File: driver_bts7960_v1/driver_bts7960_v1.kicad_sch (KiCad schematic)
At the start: 25 parts, among them J1 Motor_1, J6 Motor_2, J7 Conn_02x04_Odd_Even, U1 BTS7960B, U2 BTS7960B, U3 BTS7960B, U4 BTS7960B

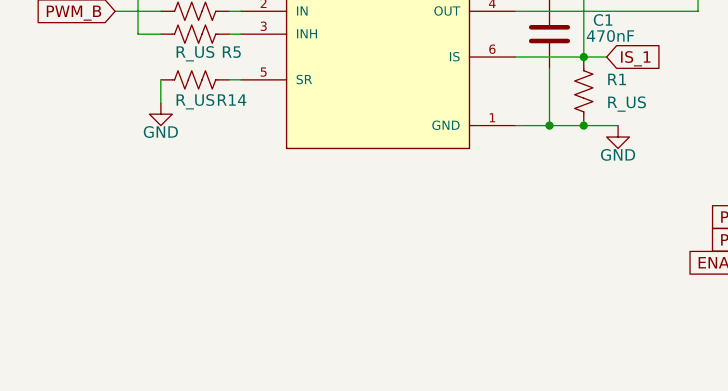
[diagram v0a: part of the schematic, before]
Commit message: driver bts7960 v1
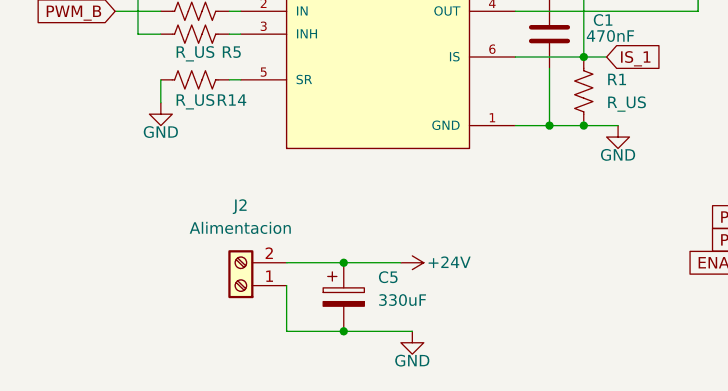
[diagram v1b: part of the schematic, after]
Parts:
- added C5: 330uF, Capacitor_THT:CP_Radial_D8.0mm_P3.80mm, symbol Device:C_Polarized
- added J2: Alimentacion, Connector_AMASS:AMASS_XT30UPB-F_1x02_P5.0mm_Vertical, symbol Connector:Screw_Terminal_01x02
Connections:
- net +24V: now also C5.1, J2.2 (Pin_2)
- net GND: now also C5.2, J2.1 (Pin_1)

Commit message: .
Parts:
- C5: footprint Capacitor_THT:CP_Radial_D8.0mm_P3.80mm -> Capacitor_THT:CP_Radial_D10.0mm_P5.00mm
- J1, J6: footprint Connector_AMASS:AMASS_XT30PW-M_1x02_P2.50mm_Horizontal -> Connector_AMASS:AMASS_XT30U-F_1x02_P5.0mm_Vertical
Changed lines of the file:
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@@
 			)
 		)
-		(property "Footprint" "Capacitor_THT:CP_Radial_D8.0mm_P3.80mm"
+		(property "Footprint" "Capacitor_THT:CP_Radial_D10.0mm_P5.00mm"
 			(at 67.0052 101.6 0)
 			(effects
@@
 			)
 		)
-		(property "Footprint" "Connector_AMASS:AMASS_XT30PW-M_1x02_P2.50mm_Horizontal"
+		(property "Footprint" "Connector_AMASS:AMASS_XT30U-F_1x02_P5.0mm_Vertical"
 			(at 215.9 49.53 0)
 			(effects
@@
 			)
 		)
-		(property "Footprint" "Connector_AMASS:AMASS_XT30PW-M_1x02_P2.50mm_Horizontal"
+		(property "Footprint" "Connector_AMASS:AMASS_XT30U-F_1x02_P5.0mm_Vertical"
 			(at 116.84 49.53 0)
 			(effects

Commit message: .
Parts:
- removed J7: Conn_02x04_Odd_Even, Connector_PinHeader_2.54mm:PinHeader_2x04_P2.54mm_Horizontal, symbol Connector_Generic:Conn_02x04_Odd_Even
- added J3: Conn_02x03_Odd_Even, Connector_PinHeader_2.54mm:PinHeader_2x03_P2.54mm_Horizontal, symbol Connector_Generic:Conn_02x03_Odd_Even
- added U5: 74HC244, Package_SO:SSOP-20_4.4x6.5mm_P0.65mm, symbol 74xx:74HC244
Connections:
- net ENABLE_1: now also J3.5 (Pin_5)
- net ENABLE_2: now also J3.6 (Pin_6)
- net GND: now also U5.10 (GND), U5.11 (2A3), U5.13 (2A2), U5.15 (2A1), U5.17 (2A0), U5.3 (2Y0), U5.5 (2Y1), U5.7 (2Y2), U5.9 (2Y3)
- net PWM_A: now also J3.1 (Pin_1), U5.2 (1A0); no longer R3.2
- net PWM_B: now also J3.3 (Pin_3), U5.4 (1A1); no longer R2.2
- net PWM_C: now also J3.2 (Pin_2), U5.6 (1A2); no longer R6.2
- net PWM_D: now also J3.4 (Pin_4), U5.8 (1A3); no longer R8.2
- net IS_1: no longer names the net of R1.1, U1.6 (IS), U2.6 (IS)
- net IS_2: no longer names the net of R10.1, U3.6 (IS), U4.6 (IS)
- new net +5V: U5.20 (VCC)
- new net OUT_A: R3.2, U5.18 (1Y0)
- new net OUT_B: R2.2, U5.16 (1Y1)
- new net OUT_C: R6.2, U5.14 (1Y2)
- new net OUT_D: R8.2, U5.12 (1Y3)

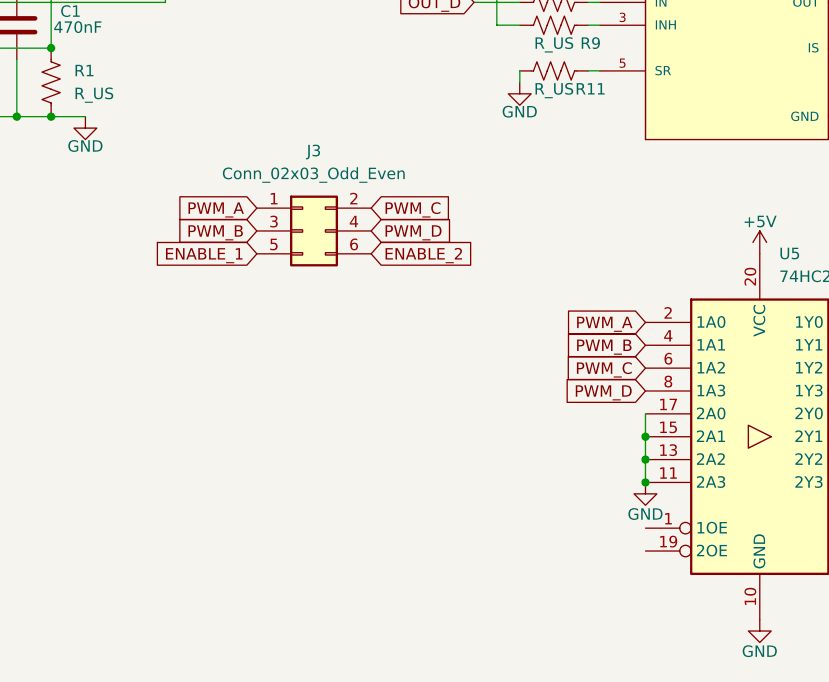
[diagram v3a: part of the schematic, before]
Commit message: v2 terminado con 74hc244
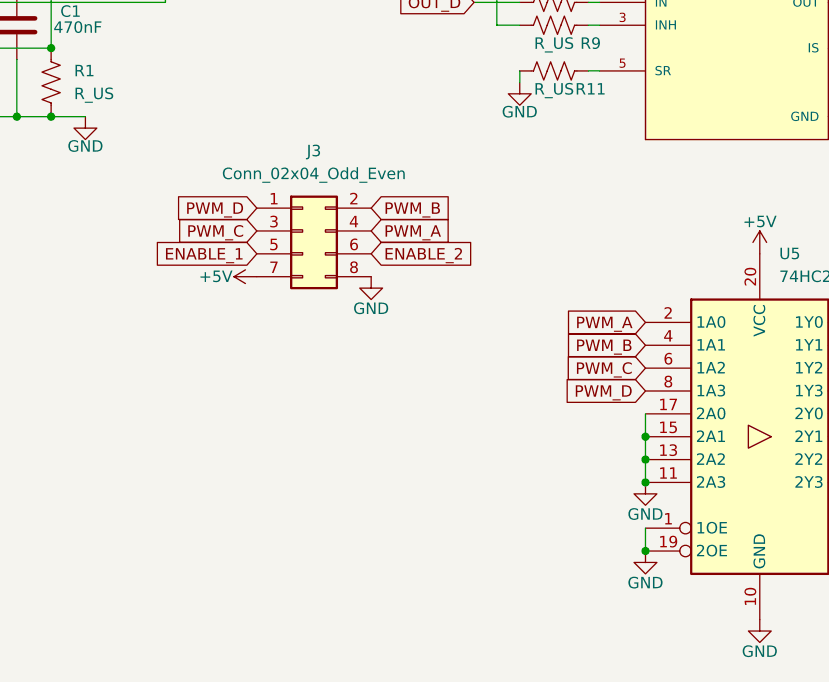
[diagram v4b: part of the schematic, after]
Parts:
- removed J3: Conn_02x03_Odd_Even, Connector_PinHeader_2.54mm:PinHeader_2x03_P2.54mm_Horizontal, symbol Connector_Generic:Conn_02x03_Odd_Even
- added J3: Conn_02x04_Odd_Even, Connector_PinHeader_2.54mm:PinHeader_2x04_P2.54mm_Vertical, symbol Connector_Generic:Conn_02x04_Odd_Even
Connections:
- net +5V: now also J3.7 (Pin_7)
- net ENABLE_1: now also J3.5 (Pin_5)
- net ENABLE_2: now also J3.6 (Pin_6)
- net GND: now also U5.1 (1OE), U5.19 (2OE), J3.8 (Pin_8)
- net PWM_A: now also J3.4 (Pin_4)
- net PWM_B: now also J3.2 (Pin_2)
- net PWM_C: now also J3.3 (Pin_3)
- net PWM_D: now also J3.1 (Pin_1)

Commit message: .
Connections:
- net ENABLE_1: now also U5.17 (2A0); no longer R4.2, R5.2
- net ENABLE_2: now also U5.15 (2A1); no longer R7.2, R9.2
- net GND: no longer U5.15 (2A1), U5.17 (2A0), U5.3 (2Y0), U5.5 (2Y1)
- new net OUT_EN_1: R4.2, R5.2, U5.3 (2Y0)
- new net OUT_EN_2: R7.2, R9.2, U5.5 (2Y1)
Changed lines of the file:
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@@
-	)
-	(junction
-		(at 184.15 114.3)
-		(diameter 0)
-		(color 0 0 0 0)
 	)
 	(junction
@@
 	)
 	(junction
-		(at 184.15 116.84)
-		(diameter 0)
-		(color 0 0 0 0)
-	)
-	(junction
 		(at 184.15 119.38)
 		(diameter 0)
@@
 	)
 	(junction
-		(at 158.75 116.84)
-		(diameter 0)
-		(color 0 0 0 0)
-	)
-	(junction
 		(at 92.71 71.12)
 		(diameter 0)
@@
 	)
 	(junction
-		(at 158.75 114.3)
-		(diameter 0)
-		(color 0 0 0 0)
-	)
-	(junction
 		(at 158.75 119.38)
 		(diameter 0)
@@
 	(wire
 		(pts
-			(xy 144.78 39.37) (xy 142.24 39.37)
-		)
-		(stroke
-			(width 0)
-			(type default)
-		)
-	)
-	(wire
-		(pts
 			(xy 53.34 68.58) (xy 54.61 68.58)
 		)
@@
 	(wire
 		(pts
-			(xy 158.75 111.76) (xy 158.75 114.3)
-		)
-		(stroke
-			(width 0)
-			(type default)
-		)
-	)
-	(wire
-		(pts
 			(xy 204.47 66.04) (xy 204.47 52.07)
 		)
@@
 	(wire
 		(pts
-			(xy 142.24 68.58) (xy 144.78 68.58)
-		)
-		(stroke
-			(width 0)
-			(type default)
-		)
-	)
-	(wire
-		(pts
 			(xy 153.67 39.37) (xy 152.4 39.37)
 		)
@@
 	(wire
 		(pts
-			(xy 43.18 39.37) (xy 43.18 68.58)
-		)
-		(stroke
-			(width 0)
-			(type default)
-		)
-	)
-	(wire
-		(pts
 			(xy 204.47 49.53) (xy 210.82 49.53)
 		)
@@
 	(wire
 		(pts
-			(xy 43.18 68.58) (xy 45.72 68.58)
-		)
-		(stroke
-			(width 0)
-			(type default)
-		)
-	)
-	(wire
-		(pts
 			(xy 187.96 60.96) (xy 187.96 64.77)
 		)
@@
 	(wire
 		(pts
-			(xy 45.72 39.37) (xy 43.18 39.37)
-		)
-		(stroke
-			(width 0)
-			(type default)
-		)
-	)
-	(wire
-		(pts
-			(xy 142.24 39.37) (xy 142.24 68.58)
-		)
-		(stroke
-			(width 0)
-			(type default)
-		)
-	)
-	(wire
-		(pts
 			(xy 152.4 68.58) (xy 153.67 68.58)
 		)
@@
 	(wire
 		(pts
-			(xy 184.15 114.3) (xy 184.15 116.84)
-		)
-		(stroke
-			(width 0)
-			(type default)
-		)
-	)
-	(wire
-		(pts
-			(xy 158.75 114.3) (xy 158.75 116.84)
-		)
-		(stroke
-			(width 0)
-			(type default)
-		)
-	)
-	(wire
-		(pts
 			(xy 184.15 41.91) (xy 191.77 41.91)
 		)
@@
 	(wire
 		(pts
-			(xy 184.15 111.76) (xy 184.15 114.3)
-		)
-		(stroke
-			(width 0)
-			(type default)
-		)
-	)
-	(wire
-		(pts
 			(xy 88.9 31.75) (xy 85.09 31.75)
 		)
@@
 		)
 	)
+	(global_label "OUT_EN_2"
+		(shape input)
+		(at 184.15 114.3 0)
+		(fields_autoplaced yes)
+		(effects
+			(font
+				(size 1.27 1.27)
+			)
+			(justify left)
+		)
+		(property "Intersheetrefs" "${INTERSHEET_REFS}"
+			(at 196.388 114.3 0)
+			(hide yes)
+			(show_name no)
+			(do_not_autoplace no)
+			(effects
+				(font
+					(size 1.27 1.27)
+				)
+				(justify left)
+			)
+		)
+	)
 	(global_label "OUT_D"
 		(shape input)
@@
 		)
 	)
+	(global_label "OUT_EN_1"
+		(shape input)
+		(at 45.72 68.58 180)
+		(fields_autoplaced yes)
+		(effects
+			(font
+				(size 1.27 1.27)
+			)
+			(justify right)
+		)
+		(property "Intersheetrefs" "${INTERSHEET_REFS}"
+			(at 33.482 68.58 0)
+			(hide yes)
+			(show_name no)
+			(do_not_autoplace no)
+			(effects
+				(font
+					(size 1.27 1.27)
+				)
+				(justify right)
+			)
+		)
+	)
 	(global_label "PWM_B"
 		(shape input)
@@
 		)
 	)
+	(global_label "ENABLE_1"
+		(shape input)
+		(at 158.75 111.76 180)
+		(fields_autoplaced yes)
+		(effects
+			(font
+				(size 1.27 1.27)
+			)
+			(justify right)
+		)
+		(property "Intersheetrefs" "${INTERSHEET_REFS}"
+			(at 146.5725 111.76 0)
+			(hide yes)
+			(show_name no)
+			(do_not_autoplace no)
+			(effects
+				(font
+					(size 1.27 1.27)
+				)
+				(justify right)
+			)
+		)
+	)
 	(global_label "OUT_B"
 		(shape input)
@@
 		)
 	)
-	(global_label "ENABLE_1"
-		(shape input)
-		(at 43.18 53.34 180)
-		(fields_autoplaced yes)
-		(effects
-			(font
-				(size 1.27 1.27)
-			)
-			(justify right)
-		)
-		(property "Intersheetrefs" "${INTERSHEET_REFS}"
-			(at 31.0025 53.34 0)
+	(global_label "OUT_EN_2"
+		(shape input)
+		(at 144.78 68.58 180)
+		(fields_autoplaced yes)
+		(effects
+			(font
+				(size 1.27 1.27)
+			)
+			(justify right)
+		)
+		(property "Intersheetrefs" "${INTERSHEET_REFS}"
+			(at 132.542 68.58 0)
+			(hide yes)
+			(show_name no)
+			(do_not_autoplace no)
+			(effects
+				(font
+					(size 1.27 1.27)
+				)
+				(justify right)
+			)
+		)
+	)
+	(global_label "OUT_EN_1"
+		(shape input)
+		(at 45.72 39.37 180)
+		(fields_autoplaced yes)
+		(effects
+			(font
+				(size 1.27 1.27)
+			)
+			(justify right)
+		)
+		(property "Intersheetrefs" "${INTERSHEET_REFS}"
+			(at 33.482 39.37 0)
 			(hide yes)
 			(show_name no)
@@
 		)
 	)
+	(global_label "ENABLE_2"
+		(shape input)
+		(at 158.75 114.3 180)
+		(fields_autoplaced yes)
+		(effects
+			(font
+				(size 1.27 1.27)
+			)
+			(justify right)
+		)
+		(property "Intersheetrefs" "${INTERSHEET_REFS}"
+			(at 146.5725 114.3 0)
+			(hide yes)
+			(show_name no)
+			(do_not_autoplace no)
+			(effects
+				(font
+					(size 1.27 1.27)
+				)
+				(justify right)
+			)
+		)
+	)
 	(global_label "PWM_C"
 		(shape input)
@@
 		)
 	)
-	(global_label "ENABLE_2"
-		(shape input)
-		(at 142.24 53.34 180)
-		(fields_autoplaced yes)
-		(effects
-			(font
-				(size 1.27 1.27)
-			)
-			(justify right)
-		)
-		(property "Intersheetrefs" "${INTERSHEET_REFS}"
-			(at 130.0625 53.34 0)
-			(hide yes)
-			(show_name no)
+	(global_label "OUT_EN_1"
+		(shape input)
+		(at 184.15 111.76 0)
+		(fields_autoplaced yes)
+		(effects
+			(font
+				(size 1.27 1.27)
+			)
+			(justify left)
+		)
+		(property "Intersheetrefs" "${INTERSHEET_REFS}"
+			(at 196.388 111.76 0)
+			(hide yes)
+			(show_name no)
+			(do_not_autoplace no)
+			(effects
+				(font
+					(size 1.27 1.27)
+				)
+				(justify left)
+			)
+		)
+	)
+	(global_label "OUT_EN_2"
+		(shape input)
+		(at 144.78 39.37 180)
+		(fields_autoplaced yes)
+		(effects
+			(font
+				(size 1.27 1.27)
+			)
+			(justify right)
+		)
+		(property "Intersheetrefs" "${INTERSHEET_REFS}"
+			(at 132.542 39.37 0)
+			(hide yes)
+			(show_name no)

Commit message: .
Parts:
- removed J3: Conn_02x04_Odd_Even, Connector_PinHeader_2.54mm:PinHeader_2x04_P2.54mm_Vertical, symbol Connector_Generic:Conn_02x04_Odd_Even
- added J7: Conn_02x04_Odd_Even, Connector_PinHeader_2.54mm:PinHeader_2x04_P2.54mm_Vertical, symbol Connector_Generic:Conn_02x04_Odd_Even
- C5: footprint Capacitor_THT:CP_Radial_D10.0mm_P5.00mm -> Capacitor_THT:CP_Radial_D8.0mm_P3.80mm
- J2: value Alimentacion -> XT30; footprint Connector_AMASS:AMASS_XT30UPB-F_1x02_P5.0mm_Vertical -> Connector_AMASS:AMASS_XT30U-F_1x02_P5.0mm_Vertical
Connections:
- net +5V: now also J7.7 (Pin_7)
- net ENABLE_1: now also J7.5 (Pin_5)
- net ENABLE_2: now also J7.6 (Pin_6)
- net GND: now also J7.8 (Pin_8)
- net PWM_A: now also J7.4 (Pin_4)
- net PWM_B: now also J7.2 (Pin_2)
- net PWM_C: now also J7.1 (Pin_1)
- net PWM_D: now also J7.3 (Pin_3)
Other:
- note added: "Control de motores"
- note added: "Entrada VCC"
- note added: "Integrado 74hc244"
- note added: "Pines de entrada"
- moved on the sheet: C1, C2, C3, C4, C5, J1, J2, J6, R1, R10, R11, R12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

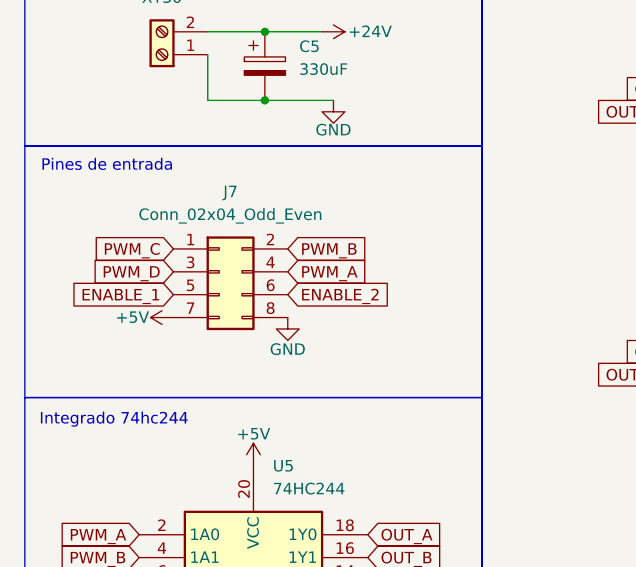
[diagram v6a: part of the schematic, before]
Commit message: footprint 74hc244 corregido
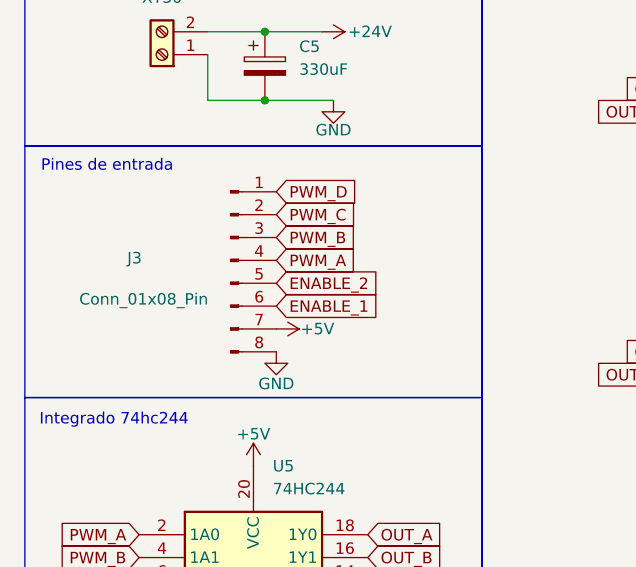
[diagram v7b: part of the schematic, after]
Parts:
- removed J7: Conn_02x04_Odd_Even, Connector_PinHeader_2.54mm:PinHeader_2x04_P2.54mm_Vertical, symbol Connector_Generic:Conn_02x04_Odd_Even
- added J3: Conn_01x08_Pin, Connector_PinHeader_2.54mm:PinHeader_1x08_P2.54mm_Vertical, symbol Connector:Conn_01x08_Pin
- U5: footprint Package_SO:SSOP-20_4.4x6.5mm_P0.65mm -> 74HC244D_653:SOIC127P1032X265-20N
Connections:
- net +5V: now also J3.7 (Pin_7)
- net ENABLE_1: now also J3.6 (Pin_6)
- net ENABLE_2: now also J3.5 (Pin_5)
- net GND: now also J3.8 (Pin_8)
- net PWM_A: now also J3.4 (Pin_4)
- net PWM_B: now also J3.3 (Pin_3)
- net PWM_C: now also J3.2 (Pin_2)
- net PWM_D: now also J3.1 (Pin_1)
